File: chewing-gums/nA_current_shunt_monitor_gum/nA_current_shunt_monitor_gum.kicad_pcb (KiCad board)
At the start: 4 copper layers, 15.2 x 27.9 mm, 37 parts, among them IC6 INA212AIDCKR, J1 Conn_Coaxial, J2 Conn_01x03, J3 Conn_01x03, J44 Conn_02x03_Odd_Even, J6 Conn_02x01, J7 Conn_02x01, SW4 SW_SPDT, U1 TLV75801PDBV, U10 LM321, U2 ADS1219, U3 TLV75801PDBV, U4 MCP4726

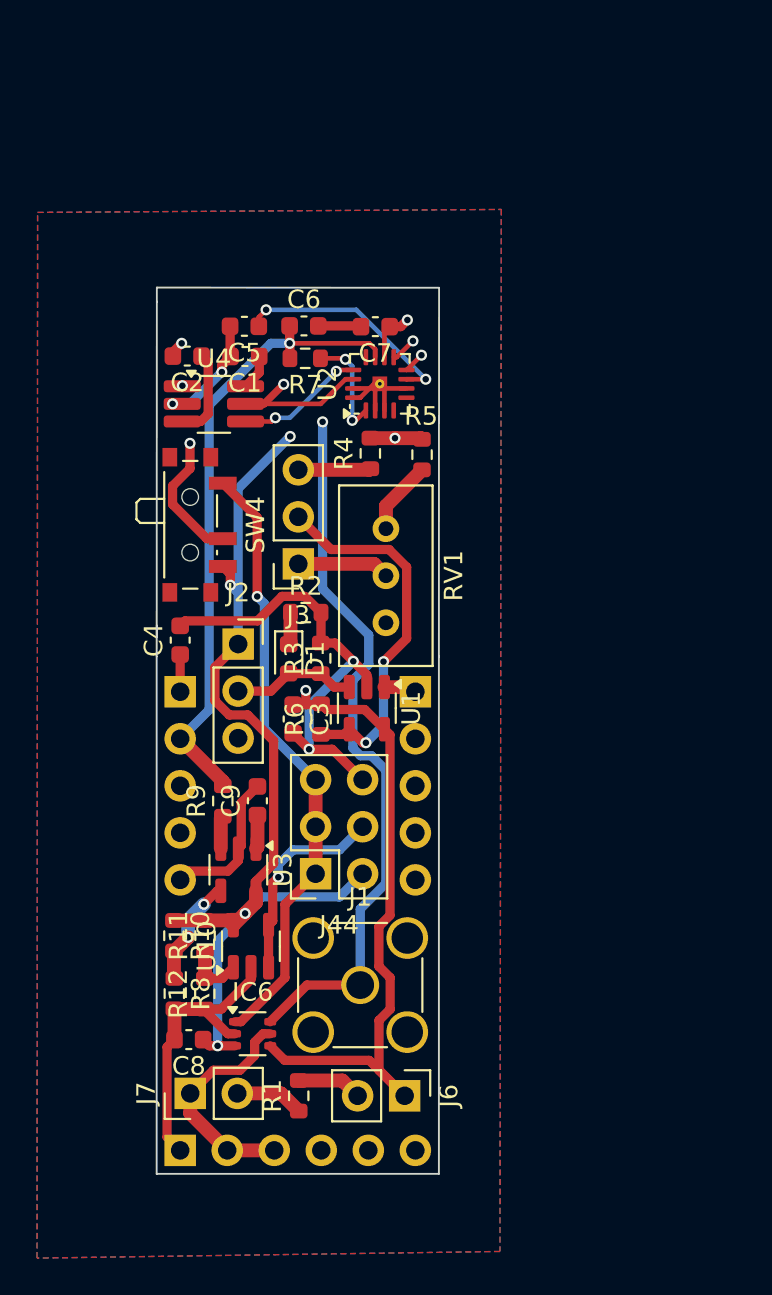
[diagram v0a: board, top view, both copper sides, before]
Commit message: adding EEPROM in sch + fix symbol connector gum
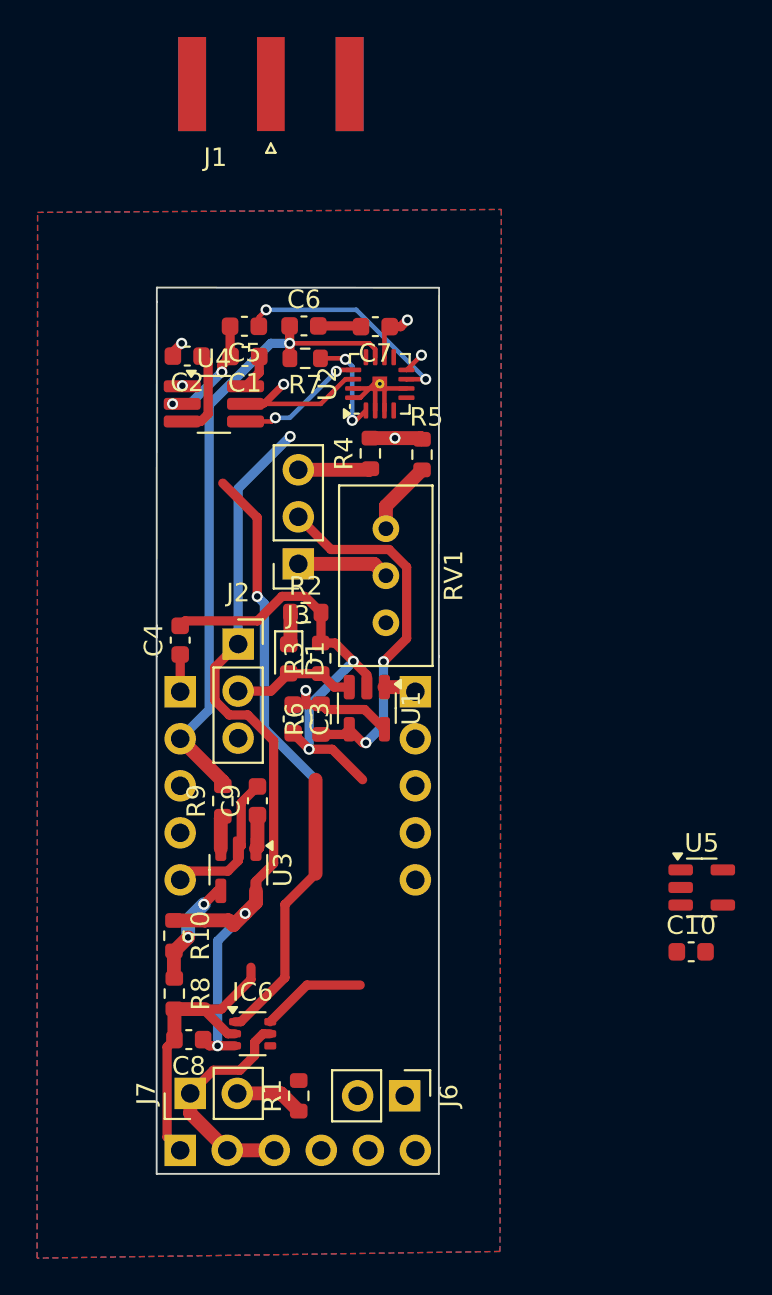
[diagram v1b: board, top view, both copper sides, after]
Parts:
- removed J44: Conn_02x03_Odd_Even, Connector_PinSocket_2.54mm:PinSocket_2x03_P2.54mm_Vertical
- removed R11, R12: 500, Resistor_SMD:R_0603_1608Metric
- removed SW4: SW_SPDT, Button_Switch_SMD:SW_SPDT_PCM12
- removed U10: LM321, Package_TO_SOT_SMD:SOT-23-5
- added C10: 0.1u, Capacitor_SMD:C_0603_1608Metric, F.Cu at (150.9, 100.5)
- added U5: 24AA02E-OT, Package_TO_SOT_SMD:SOT-23-5, F.Cu at (151.5, 97.1)
- J1: footprint Connector_Coaxial:SMA_Amphenol_901-144_Vertical -> Connector_Coaxial:SMA_Amphenol_132289_EdgeMount
- moved J1 48.9 mm to (128.2, 53.7), turned to 90 degrees
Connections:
- C5 pad 1: Net-(SW4-B) -> A3.3V
- IC6 pad 1: /REF_INA -> GND
- U2 pad 7: Net-(SW4-B) -> A3.3V
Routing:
- net /ADC0: track 47.2 -> 5.68 mm, vias 2 -> 0
- net /REF_INA: track 33.1 -> 0.00 mm, vias 1 -> 0
- net GND: track 67.8 -> 100.9 mm, vias 5 -> 6
- net /V_LSL_LDO: track 57.9 -> 28.3 mm
- net Net-(SW4-B): track 28.3 -> 0.00 mm, vias 3 -> 0
- net Net-(J44-Pin_4): track 11.5 -> 0.00 mm, vias 1 -> 0
- net Net-(J6-Pin_2): track 3.52 -> 0.00 mm
- net Net-(U10-+): track 3.29 -> 0.00 mm
- net A3.3V: track 64.8 -> 67.9 mm, vias 5 -> 6

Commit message: Finish gum pcb layout with EEPROM
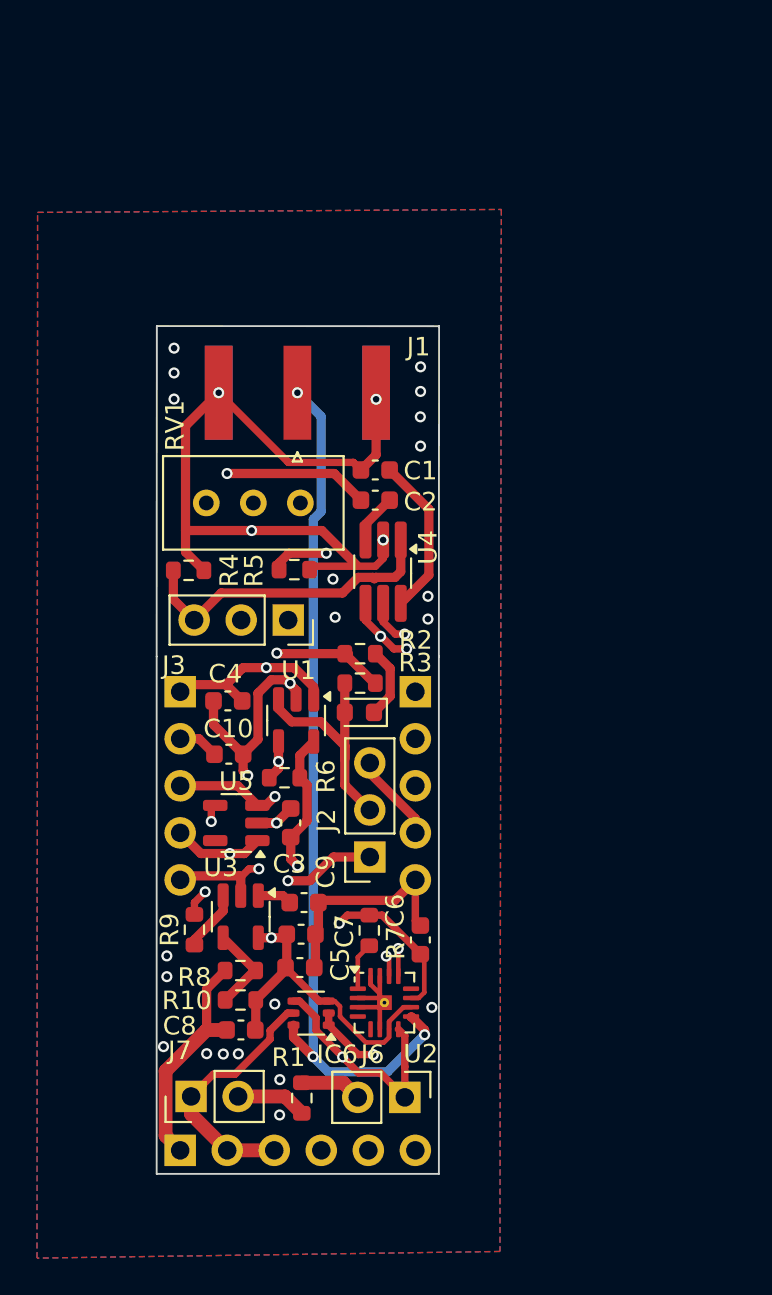
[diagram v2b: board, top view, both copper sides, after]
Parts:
- moved C5 34.8 mm to (129.8, 101.4), turned to 0 degrees
- moved C6 33.7 mm to (136.3, 99.9), turned to 90 degrees
- moved U2 33.4 mm to (134.3, 103.3), turned to 0 degrees
- moved C7 33.1 mm to (129.8, 99.6), turned to 0 degrees
- moved R7 31.1 mm to (133.5, 99.4), turned to 90 degrees
- moved C10 27.2 mm to (125.9, 89.9)
- moved U5 25.4 mm to (126.3, 93.6), turned to 180 degrees
- moved J1 16.7 mm to (129.7, 70.3)
- moved J2 13.5 mm to (133.6, 95.4), turned to 180 degrees
- moved U4 12.9 mm to (134.3, 80.0), turned to -90 degrees
- moved C2 12.8 mm to (133.9, 76.1)
- moved R4 11.7 mm to (123.8, 79.9), turned to 0 degrees
- moved RV1 11.7 mm to (124.7, 76.3), turned to 180 degrees
- moved C1 9.33 mm to (133.9, 74.5)
- moved R5 9.28 mm to (129.5, 79.9), turned to 0 degrees
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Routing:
- net A3.3V: track 67.9 -> 26.0 mm, vias 6 -> 2
- net /ADC0: track 5.68 -> 47.2 mm, vias 0 -> 3
- net GND: track 100.9 -> 127.5 mm, vias 6 -> 31
- net 3.3V: track 41.5 -> 54.5 mm, vias 2 -> 4
- net /V_ldo_feedback: track 20.2 -> 10.6 mm, vias 2 -> 1
- net /SDA: track 29.3 -> 38.6 mm, vias 2 -> 4
- net /LDO_EN_EXT: track 11.7 -> 4.79 mm
- net Net-(U4-Vref): track 1.92 -> 8.72 mm
- net Net-(D1-A): track 6.70 -> 13.0 mm
- net /DAC_out: track 12.1 -> 17.2 mm, vias 1 -> 0
- net /V_LSL_LDO: track 28.3 -> 31.9 mm
- net Net-(J6-Pin_2): track 0.00 -> 3.35 mm
- net Net-(U2-!RESET): track 5.78 -> 2.58 mm, vias 2 -> 0
- net Net-(R5-Pad1): track 3.98 -> 6.75 mm, vias 0 -> 1
- net Net-(U4-VDD): track 4.84 -> 2.72 mm
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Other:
- board text added: "GND"

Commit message: production files
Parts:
- removed J6: Conn_02x01, Connector_PinHeader_2.54mm:PinHeader_1x02_P2.54mm_Vertical
- added G***: LOGO, heep-footprints:EPFL_3x1, B.Cu at (126.7, 79.4)
- added G***: LOGO, heep-footprints:ESL_3x3, B.Cu at (131.3, 105.7)
- added R11: 10, Resistor_SMD:R_2010_5025Metric_Pad1.40x2.65mm_HandSolder, B.Cu at (127.6, 102.8)
- added R12: 10, Resistor_SMD:R_1206_3216Metric_Pad1.30x1.75mm_HandSolder, B.Cu at (124.8, 102.2)
- added R13: 1M, Resistor_SMD:R_0402_1005Metric, F.Cu at (129.6, 106.1)
- added R14: 10, Resistor_SMD:R_2512_6332Metric_Pad1.40x3.35mm_HandSolder, B.Cu at (124.0, 102.2)
- added TP14: 5029, TestPoint:TestPoint_Keystone_5019_Miniature, F.Cu at (123.7, 69.2)
- added TP2: ~, TestPoint:TestPoint_Loop_D1.80mm_Drill1.0mm_Beaded, F.Cu at (132.6, 108.8)
- J2, J3: footprint Connector_PinSocket_2.54mm:PinSocket_1x03_P2.54mm_Vertical -> Connector_PinHeader_2.54mm:PinHeader_1x03_P2.54mm_Vertical
- J7: footprint Connector_PinHeader_2.54mm:PinHeader_1x02_P2.54mm_Vertical -> Connector_PinHeader_2.54mm:PinHeader_1x03_P2.54mm_Vertical
- R1: footprint Resistor_SMD:R_0603_1608Metric -> Resistor_SMD:R_0805_2012Metric_Pad1.20x1.40mm_HandSolder; moved to B.Cu
- U4: footprint Package_TO_SOT_SMD:TSOT-23-6_HandSoldering -> Package_TO_SOT_SMD:TSOT-23-6
- moved C1 8.97 mm to (135.9, 83.2), turned to -90 degrees
- moved R1 6.26 mm to (127.1, 102.8)
- moved J1 2.31 mm to (131.7, 69.3)
- moved U4 0.64 mm to (134.1, 79.4)
- moved C2 0.28 mm to (134.1, 76.3), turned to 0 degrees
- moved J7 0.06 mm to (123.9, 108.4)
- turned R5 to 180 degrees
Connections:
- C1 pad 1: Net-(U4-Vref) -> A3.3V
- C2 pad 1: Net-(U4-VDD) -> 3.3V
- C2 pad 2: 3.3V -> GND
- C9 pad 1: Net-(U3-IN) -> /5V
- IC6 pad 5: /V_LSL_load -> /Shunt-
- J2 pad 1: A3.3V -> /5V
- J7 pad 2: Net-(J7-Pin_2) -> /Shunt-
- R1 pad 1: Net-(J7-Pin_2) -> /Shunt-
- R1 pad 2: Net-(J6-Pin_2) -> /V_LSL_LDO
- U3 pad 1: Net-(U3-IN) -> /5V
- U4 pad 3: Net-(U4-VDD) -> 3.3V
- U4 pad 6: Net-(U4-Vref) -> A3.3V
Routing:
- net GND: track 127.5 -> 162.3 mm, vias 31 -> 30
- net /5V: track 19.0 -> 37.3 mm
- net /Shunt-: track 0.00 -> 18.1 mm, vias 0 -> 1
- net A3.3V: track 26.0 -> 42.9 mm
- net /V_LSL_load: track 13.9 -> 28.5 mm
- net /V_LSL_LDO: track 31.9 -> 43.2 mm, vias 2 -> 5
- net Net-(U4-Vref): track 8.72 -> 0.00 mm
- net /SDA: track 38.6 -> 34.2 mm
- net Net-(J7-Pin_2): track 3.82 -> 0.00 mm
- net Net-(J7-Pin_3): track 0.00 -> 3.59 mm
- net Net-(J6-Pin_2): track 3.35 -> 0.00 mm
- net Net-(U4-VDD): track 2.72 -> 0.00 mm
- net /ADC0: track 47.2 -> 49.5 mm, vias 3 -> 2
- net 3.3V: track 54.5 -> 56.6 mm
- net Net-(U3-IN): track 1.85 -> 0.00 mm
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- added copper zone on B.Cu, net /V_LSL_LDO
- added copper zone on F.Cu, net /V_LSL_LDO
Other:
- board text added: "ESL 2025"
- board text added: "I-trace output"
- board text added: "INA21[x]"
- board text added: "Programmable supply & current monitor"
- board text added: "SHUNT R (Ohms)"
- board text added: "VLDO"
- board text added: "x=[0|1|2|3|4|5]"
